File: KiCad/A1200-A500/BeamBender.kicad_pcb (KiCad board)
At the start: 4 copper layers, 50 x 100 mm, 68 parts, among them J1 4-1734742-0, J2 HDMI_A_1.4, J3 STX-3501-3N, J4 Phoenix_Contact, U1 LM1117-3.3, U2 GW1NR-UV9LQ144P, U3 ADV7513BSWZ, U4 MCP1702T-1802E_CB, X1 Abracon ASE-27.000MHZ-L-R-T, X2 Oscillator_7.0x5.0mm

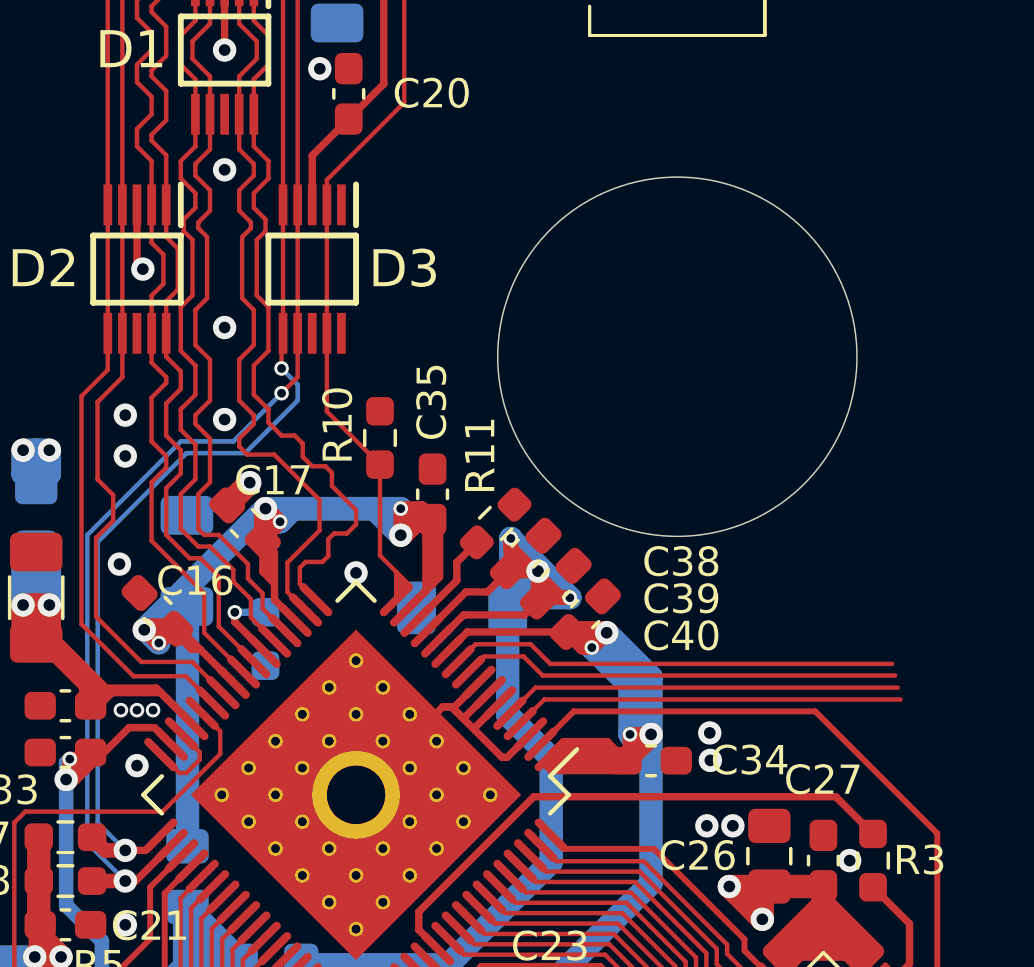
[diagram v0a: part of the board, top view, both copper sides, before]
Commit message: Changed PD to pull-up instead of pull-down, fixed A1200 mounting hole and A500 cutout area
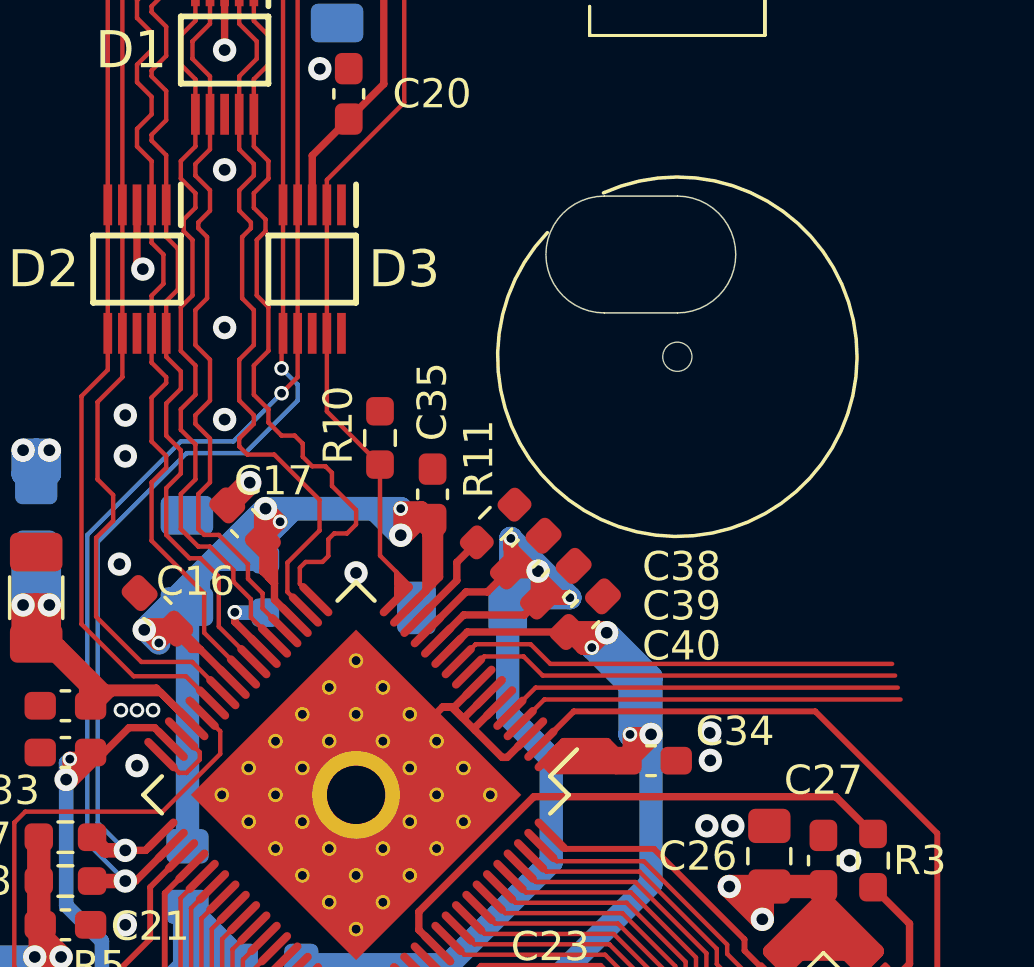
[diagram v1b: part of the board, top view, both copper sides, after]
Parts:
- added J5: Conn_01x01, Connector_PinSocket_2.54mm:PinSocket_1x01_P2.54mm_Vertical, F.Cu at (123.1, 67.2)
- moved R9 1.81 mm to (109.0, 75.1), turned to 90 degrees
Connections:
- R9 pad 2: GND -> AVDD
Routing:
- net AVDD: track 59.7 -> 65.3 mm
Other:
- outline, holes or cut-outs redrawn

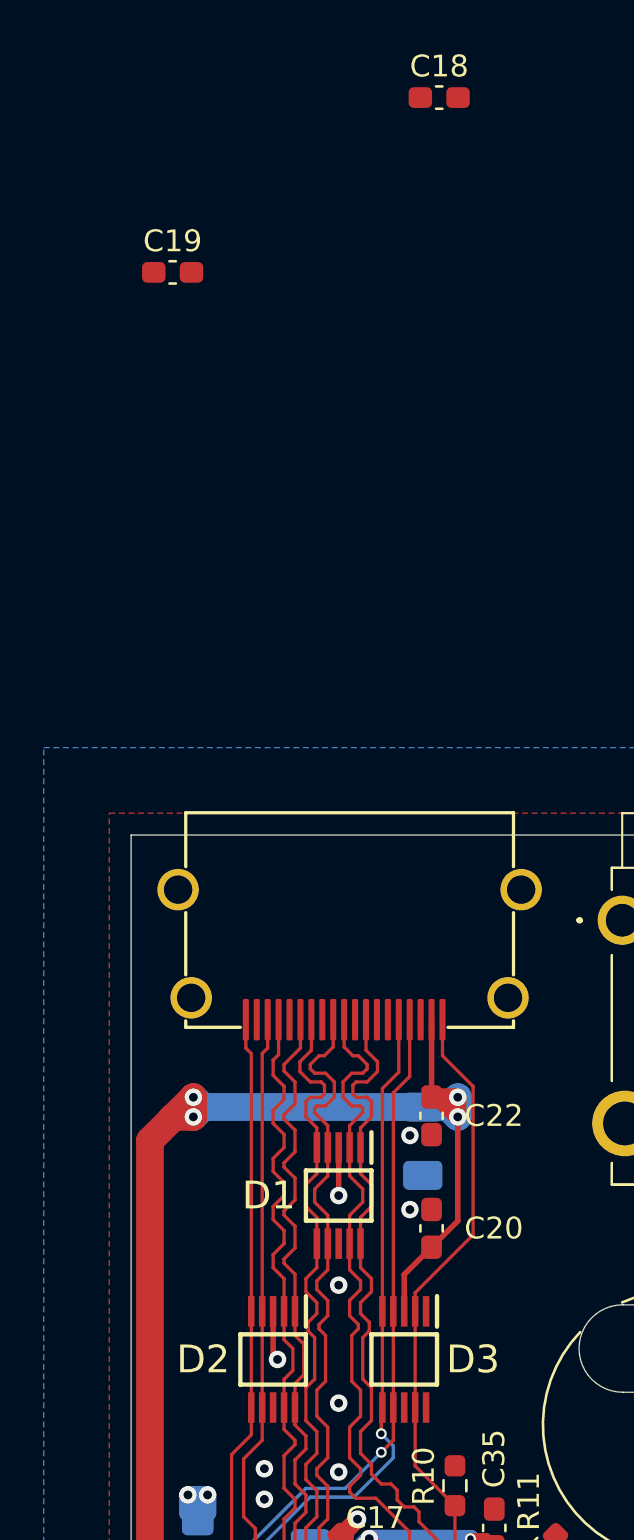
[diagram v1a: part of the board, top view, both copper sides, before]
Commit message: Placement of C18,C19
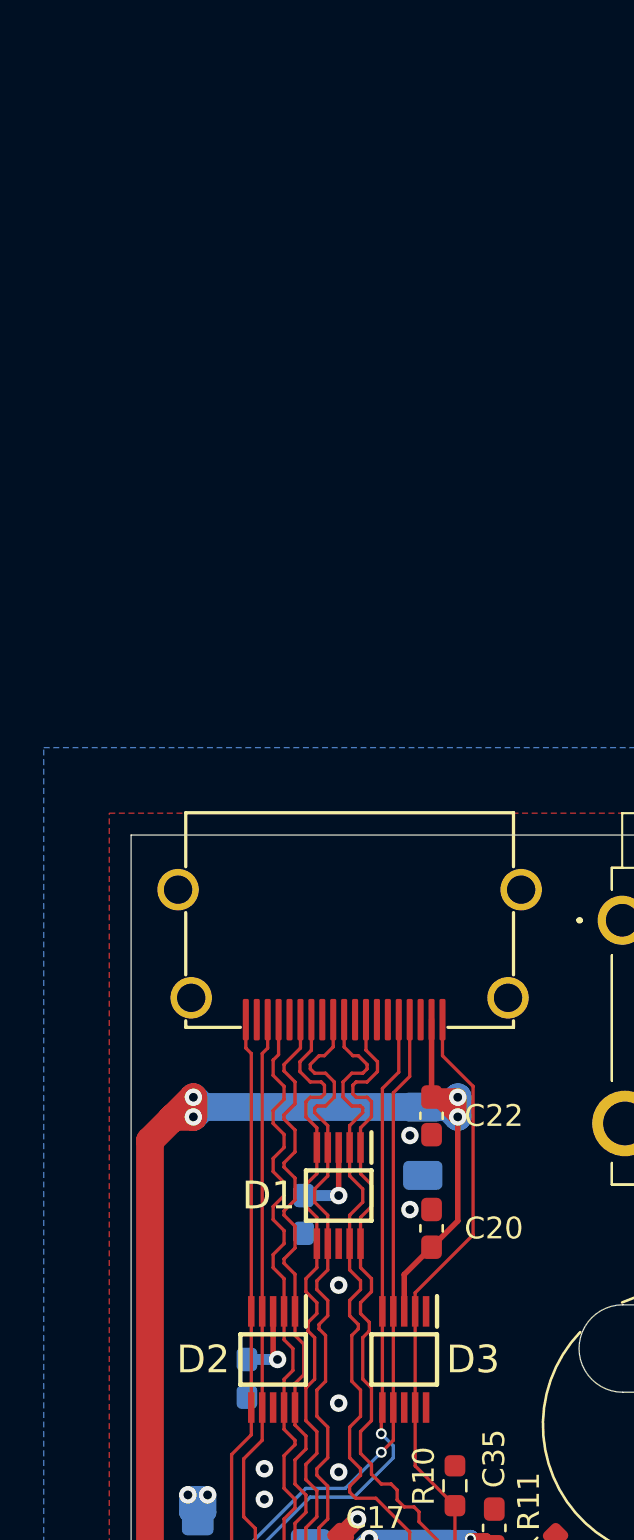
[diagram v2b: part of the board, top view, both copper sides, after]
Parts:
- C18, C19: moved to B.Cu
- moved C18 51.5 mm to (106.0, 57.6), turned to 270 degrees
- moved C19 50.7 mm to (103.4, 65.1), turned to 90 degrees
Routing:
- net /Vp_D1: track 2.20 -> 3.80 mm
- net /Vp_D2: track 2.28 -> 3.68 mm

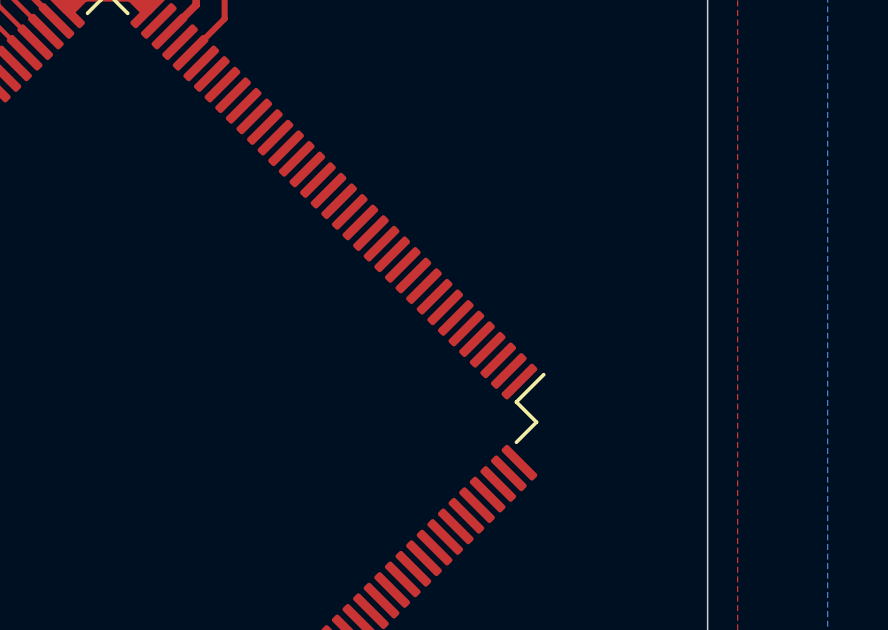
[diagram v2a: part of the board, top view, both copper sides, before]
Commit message: Breakout of own symbol for A500 drill-hole and more assignments of FPGA-pins
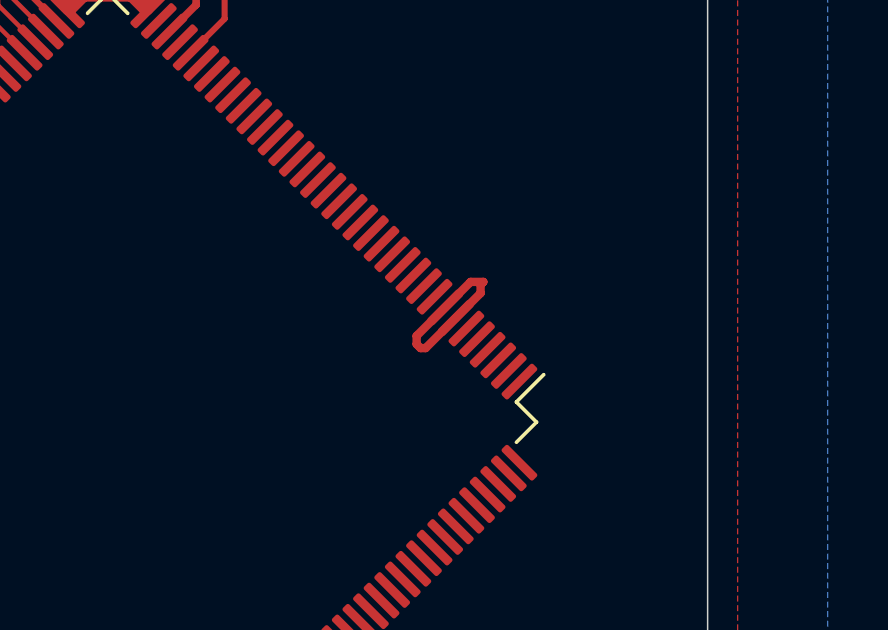
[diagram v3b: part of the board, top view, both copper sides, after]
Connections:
- net Net-(U2-Pad143) renamed MODE1
- net Net-(U2-Pad144) renamed MODE0
- U2 pad 12: Net-(U2-Pad12) -> GND
- U2 pad 122: Net-(U2-Pad122) -> GND
- U2 pad 15: SCLK -> GND
- U2 pad 23: Net-(U2-Pad23) -> GND
- U2 pad 7: JTAGSEL_N -> GND
- U2 pad 8: Net-(U2-Pad8) -> GND
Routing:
- net GND: track 19.8 -> 26.4 mm

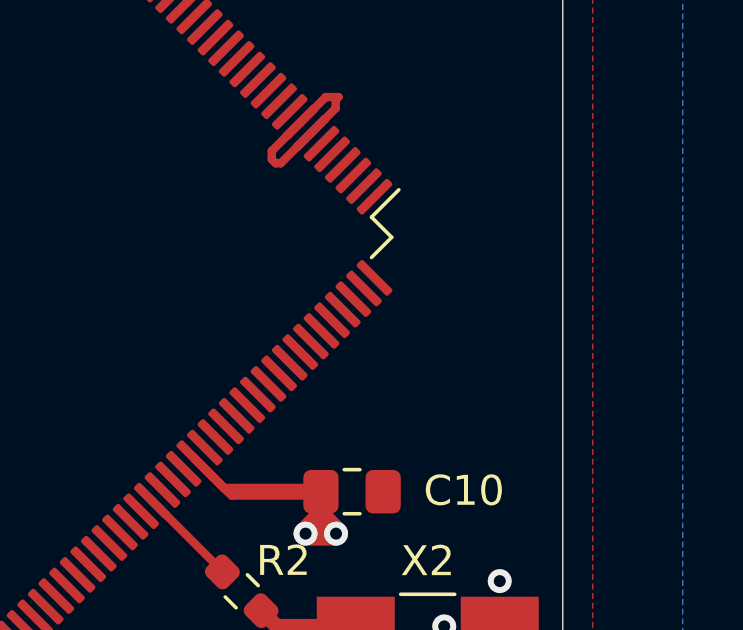
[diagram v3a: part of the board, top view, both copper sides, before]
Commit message: Added 1k pull-down resistors on the FPGA's MODE0 and MODE1 pins
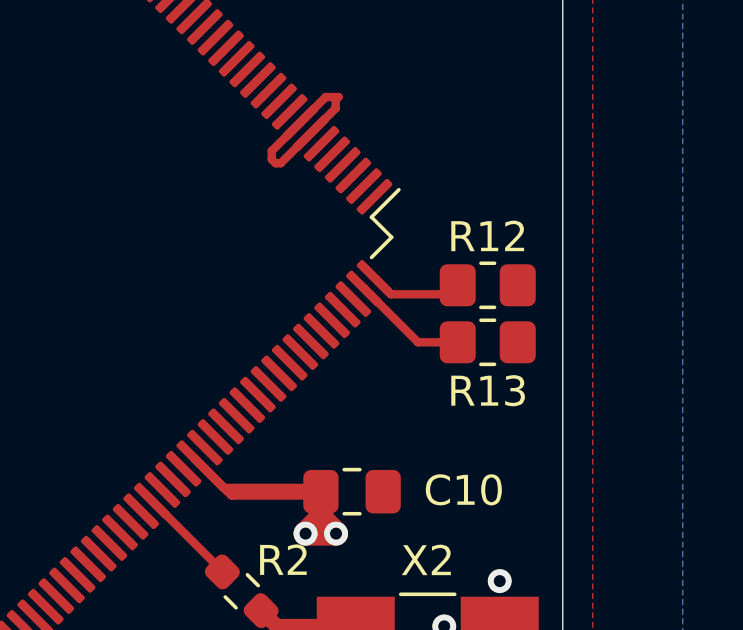
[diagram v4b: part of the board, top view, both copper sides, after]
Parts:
- added R12: 1k, Resistor_SMD:R_0805_2012Metric_Pad1.20x1.40mm_HandSolder, F.Cu at (145.6, 103.5)
- added R13: 1k, Resistor_SMD:R_0805_2012Metric_Pad1.20x1.40mm_HandSolder, F.Cu at (145.6, 105.4)
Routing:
- net MODE1: track 0.00 -> 3.87 mm
- net MODE0: track 0.00 -> 3.12 mm

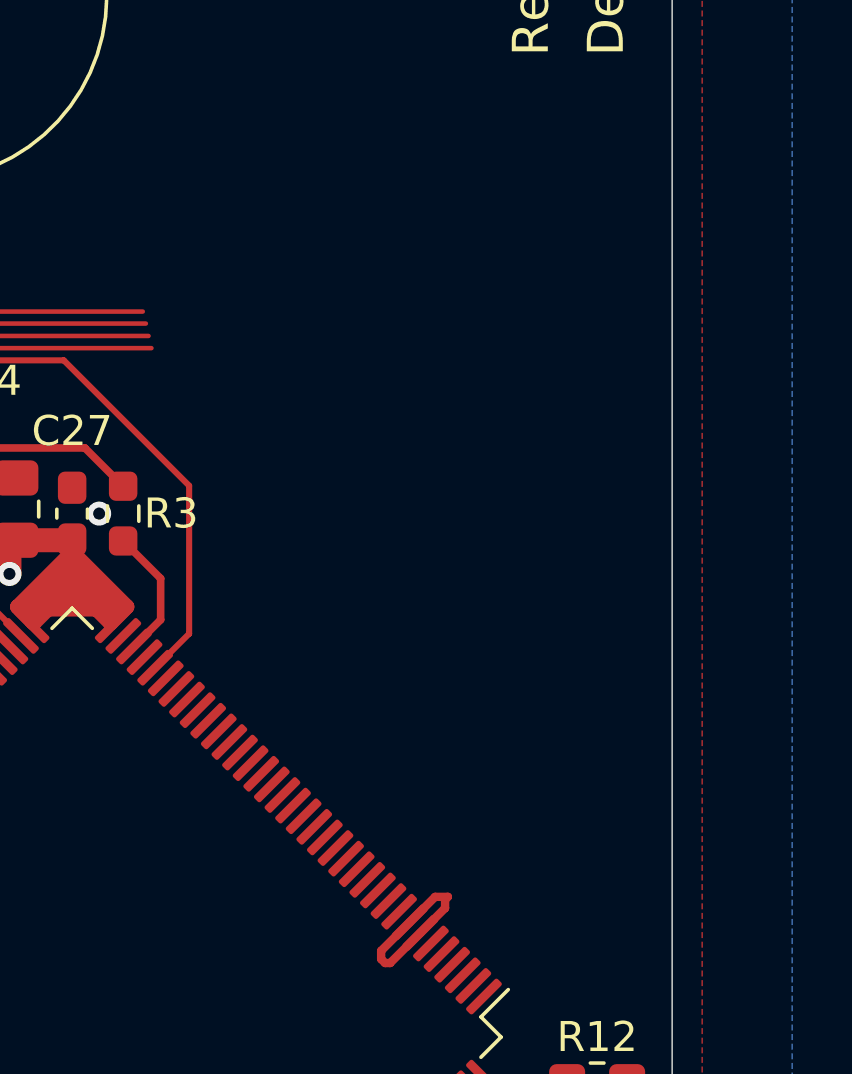
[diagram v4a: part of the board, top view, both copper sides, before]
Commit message: Added JTAG-pinheader and pull-up resistor arrays
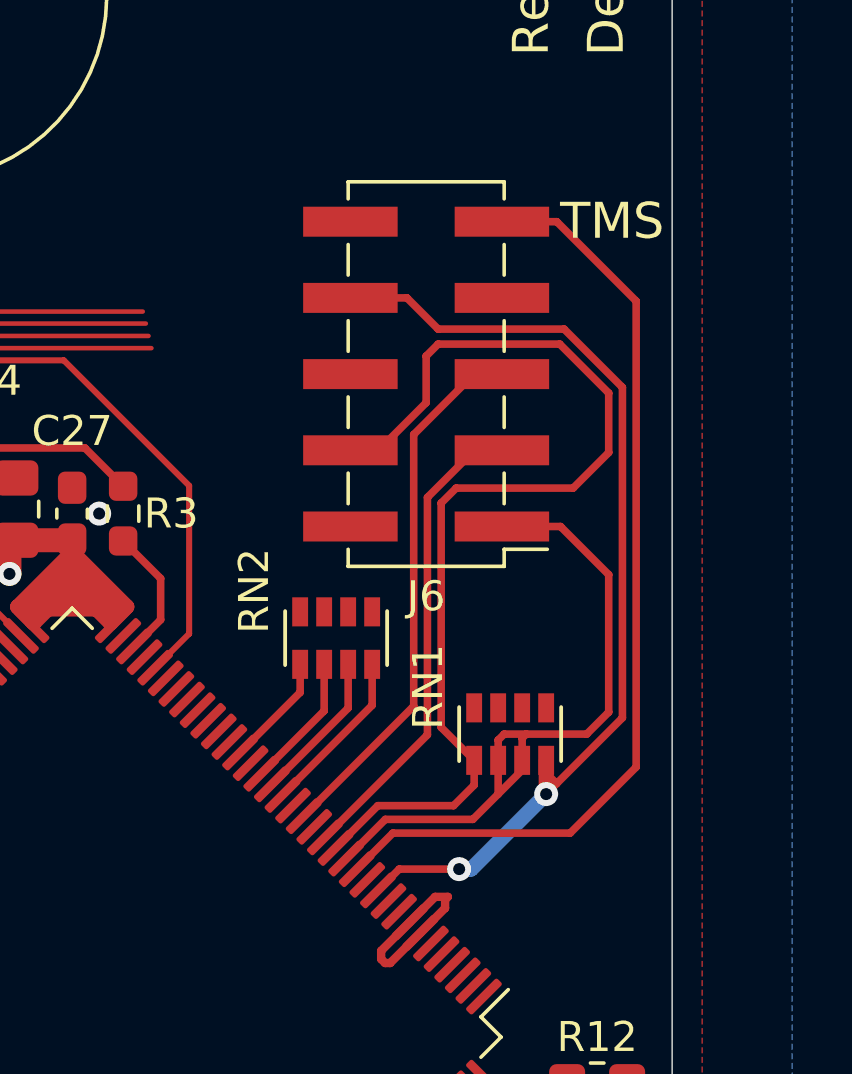
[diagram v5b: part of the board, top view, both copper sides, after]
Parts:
- added J6: Conn_02x05_Odd_Even, Connector_PinHeader_2.54mm:PinHeader_2x05_P2.54mm_Vertical_SMD, F.Cu at (139.9, 79.8)
- added RN1: 10k, BeamBender:RESCAF80P320X160X60-8N, F.Cu at (142.7, 91.8)
- added RN2: 10k, BeamBender:RESCAF80P320X160X60-8N, F.Cu at (136.9, 88.6)
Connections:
- U2 pad 11: Net-(U2-Pad11) -> JP1
- U2 pad 15: GND -> JP2
- U2 pad 24: Net-(U2-Pad24) -> JP3
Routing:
- net JP2: track 0.00 -> 35.3 mm
- net JP1: track 0.00 -> 33.9 mm, vias 0 -> 2
- net TMS: track 0.00 -> 31.8 mm
- net TCK: track 0.00 -> 23.0 mm
- net TDO: track 0.00 -> 18.0 mm
- net TDI: track 0.00 -> 15.9 mm
- net RECONFIG_N: track 0.00 -> 5.59 mm
- net DONE: track 0.00 -> 5.06 mm
- net READY: track 0.00 -> 4.52 mm
- net JP3: track 0.00 -> 3.77 mm
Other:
- board text added: "TMS"
